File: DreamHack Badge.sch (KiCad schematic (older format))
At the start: 11 parts, among them J2 Conn_01x14_Female, J4 Conn_01x04_Female, U1 ESP32-WROOM-32

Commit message: fixed footprints
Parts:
- J2: footprint (none) -> Pin_Headers:Pin_Header_Straight_1x14_Pitch2.54mm
- J4: footprint (none) -> Pin_Headers:Pin_Header_Straight_1x04_Pitch2.54mm
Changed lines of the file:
@@
 $EndComp
 $Comp
-L power:+3.3V #PWR?
+L power:+3.3V #PWR0101
 U 1 1 5CF7473F
 P 2400 1950
-F 0 "#PWR?" H 2400 1800 50  0001 C CNN
+F 0 "#PWR0101" H 2400 1800 50  0001 C CNN
 F 1 "+3.3V" H 2415 2123 50  0000 C CNN
 F 2 "" H 2400 1950 50  0001 C CNN
@@
 $EndComp
 $Comp
-L power:GND #PWR?
+L power:GND #PWR0102
 U 1 1 5CF74DDF
 P 3650 5550
-F 0 "#PWR?" H 3650 5300 50  0001 C CNN
+F 0 "#PWR0102" H 3650 5300 50  0001 C CNN
 F 1 "GND" H 3655 5377 50  0000 C CNN
 F 2 "" H 3650 5550 50  0001 C CNN
@@
 F 0 "J2" H 6228 2126 50  0000 L CNN
 F 1 "Conn_01x14_Female" H 6228 2035 50  0000 L CNN
-F 2 "" H 6200 2150 50  0001 C CNN
+F 2 "Pin_Headers:Pin_Header_Straight_1x14_Pitch2.54mm" H 6200 2150 50  0001 C CNN
 F 3 "~" H 6200 2150 50  0001 C CNN
 	1    6200 2150
@@
 Connection ~ 8400 4800
 $Comp
-L power:GND #PWR?
+L power:GND #PWR0103
 U 1 1 5CF8F9AB
 P 5750 5850
-F 0 "#PWR?" H 5750 5600 50  0001 C CNN
+F 0 "#PWR0103" H 5750 5600 50  0001 C CNN
 F 1 "GND" H 5755 5677 50  0000 C CNN
 F 2 "" H 5750 5850 50  0001 C CNN
@@
 Connection ~ 9300 4200
 $Comp
-L power:+3.3V #PWR?
+L power:+3.3V #PWR0104
 U 1 1 5CF95312
 P 10050 5250
-F 0 "#PWR?" H 10050 5100 50  0001 C CNN
+F 0 "#PWR0104" H 10050 5100 50  0001 C CNN
 F 1 "+3.3V" H 10065 5423 50  0000 C CNN
 F 2 "" H 10050 5250 50  0001 C CNN
@@
 	3650 5350 3650 5550
 $Comp
-L power:GND #PWR?
+L power:GND #PWR0105
 U 1 1 5CF9CC42
 P 5450 1650
-F 0 "#PWR?" H 5450 1400 50  0001 C CNN
+F 0 "#PWR0105" H 5450 1400 50  0001 C CNN
 F 1 "GND" H 5455 1477 50  0000 C CNN
 F 2 "" H 5450 1650 50  0001 C CNN
@@
 F 0 "J4" H 6228 3376 50  0000 L CNN
 F 1 "Conn_01x04_Female" H 6228 3285 50  0000 L CNN
-F 2 "" H 6200 3400 50  0001 C CNN
+F 2 "Pin_Headers:Pin_Header_Straight_1x04_Pitch2.54mm" H 6200 3400 50  0001 C CNN
 F 3 "~" H 6200 3400 50  0001 C CNN
 	1    6200 3400

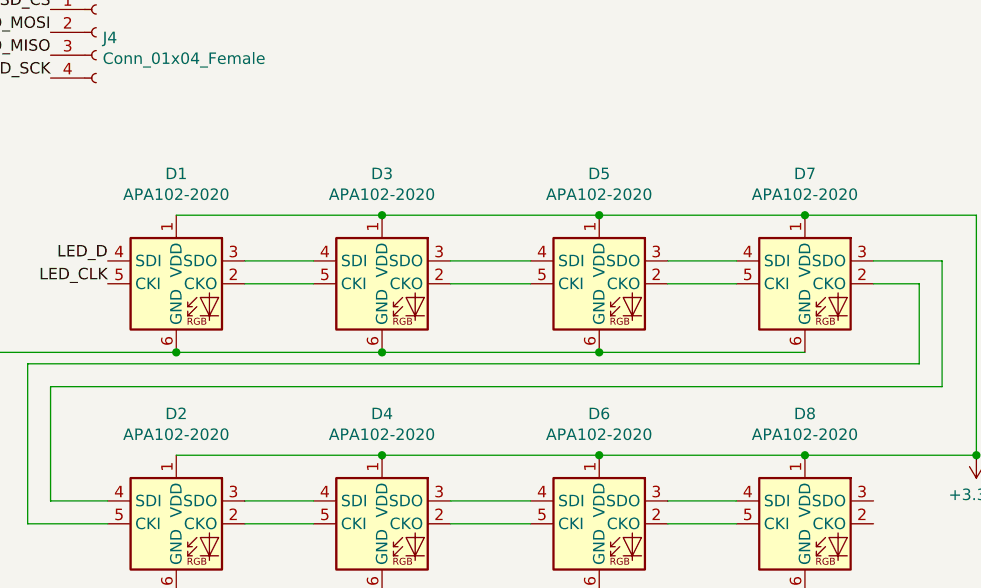
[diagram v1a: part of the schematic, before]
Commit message: fixed apa102 refs
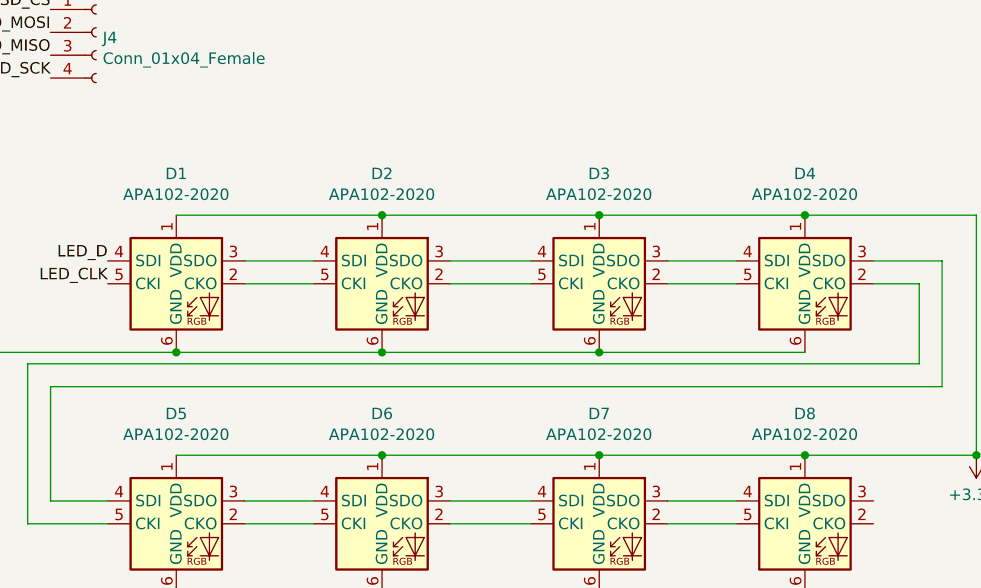
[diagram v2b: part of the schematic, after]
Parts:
- renumbered D3 to D2, D5 to D3, D7 to D4, D2 to D5, D4 to D6, D6 to D7
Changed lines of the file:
@@
 $EndComp
 $Comp
-L LED:APA102-2020 D3
+L LED:APA102-2020 D2
 U 1 1 5CF435C6
 P 7450 4500
-F 0 "D3" H 7450 4981 50  0000 C CNN
+F 0 "D2" H 7450 4981 50  0000 C CNN
 F 1 "APA102-2020" H 7450 4890 50  0000 C CNN
 F 2 "LED_SMD:LED-APA102-2020" H 7500 4200 50  0001 L TNN
@@
 $EndComp
 $Comp
-L LED:APA102-2020 D5
+L LED:APA102-2020 D3
 U 1 1 5CF440DC
 P 8400 4500
-F 0 "D5" H 8400 4981 50  0000 C CNN
+F 0 "D3" H 8400 4981 50  0000 C CNN
 F 1 "APA102-2020" H 8400 4890 50  0000 C CNN
 F 2 "LED_SMD:LED-APA102-2020" H 8450 4200 50  0001 L TNN
@@
 $EndComp
 $Comp
-L LED:APA102-2020 D7
+L LED:APA102-2020 D4
 U 1 1 5CF44F4F
 P 9300 4500
-F 0 "D7" H 9300 4981 50  0000 C CNN
+F 0 "D4" H 9300 4981 50  0000 C CNN
 F 1 "APA102-2020" H 9300 4890 50  0000 C CNN
 F 2 "LED_SMD:LED-APA102-2020" H 9350 4200 50  0001 L TNN
@@
 $EndComp
 $Comp
-L LED:APA102-2020 D2
+L LED:APA102-2020 D5
 U 1 1 5CF4E50D
 P 6550 5550
-F 0 "D2" H 6550 6031 50  0000 C CNN
+F 0 "D5" H 6550 6031 50  0000 C CNN
 F 1 "APA102-2020" H 6550 5940 50  0000 C CNN
 F 2 "LED_SMD:LED-APA102-2020" H 6600 5250 50  0001 L TNN
@@
 $EndComp
 $Comp
-L LED:APA102-2020 D4
+L LED:APA102-2020 D6
 U 1 1 5CF4E513
 P 7450 5550
-F 0 "D4" H 7450 6031 50  0000 C CNN
+F 0 "D6" H 7450 6031 50  0000 C CNN
 F 1 "APA102-2020" H 7450 5940 50  0000 C CNN
 F 2 "LED_SMD:LED-APA102-2020" H 7500 5250 50  0001 L TNN
@@
 $EndComp
 $Comp
-L LED:APA102-2020 D6
+L LED:APA102-2020 D7
 U 1 1 5CF4E519
 P 8400 5550
-F 0 "D6" H 8400 6031 50  0000 C CNN
+F 0 "D7" H 8400 6031 50  0000 C CNN
 F 1 "APA102-2020" H 8400 5940 50  0000 C CNN
 F 2 "LED_SMD:LED-APA102-2020" H 8450 5250 50  0001 L TNN

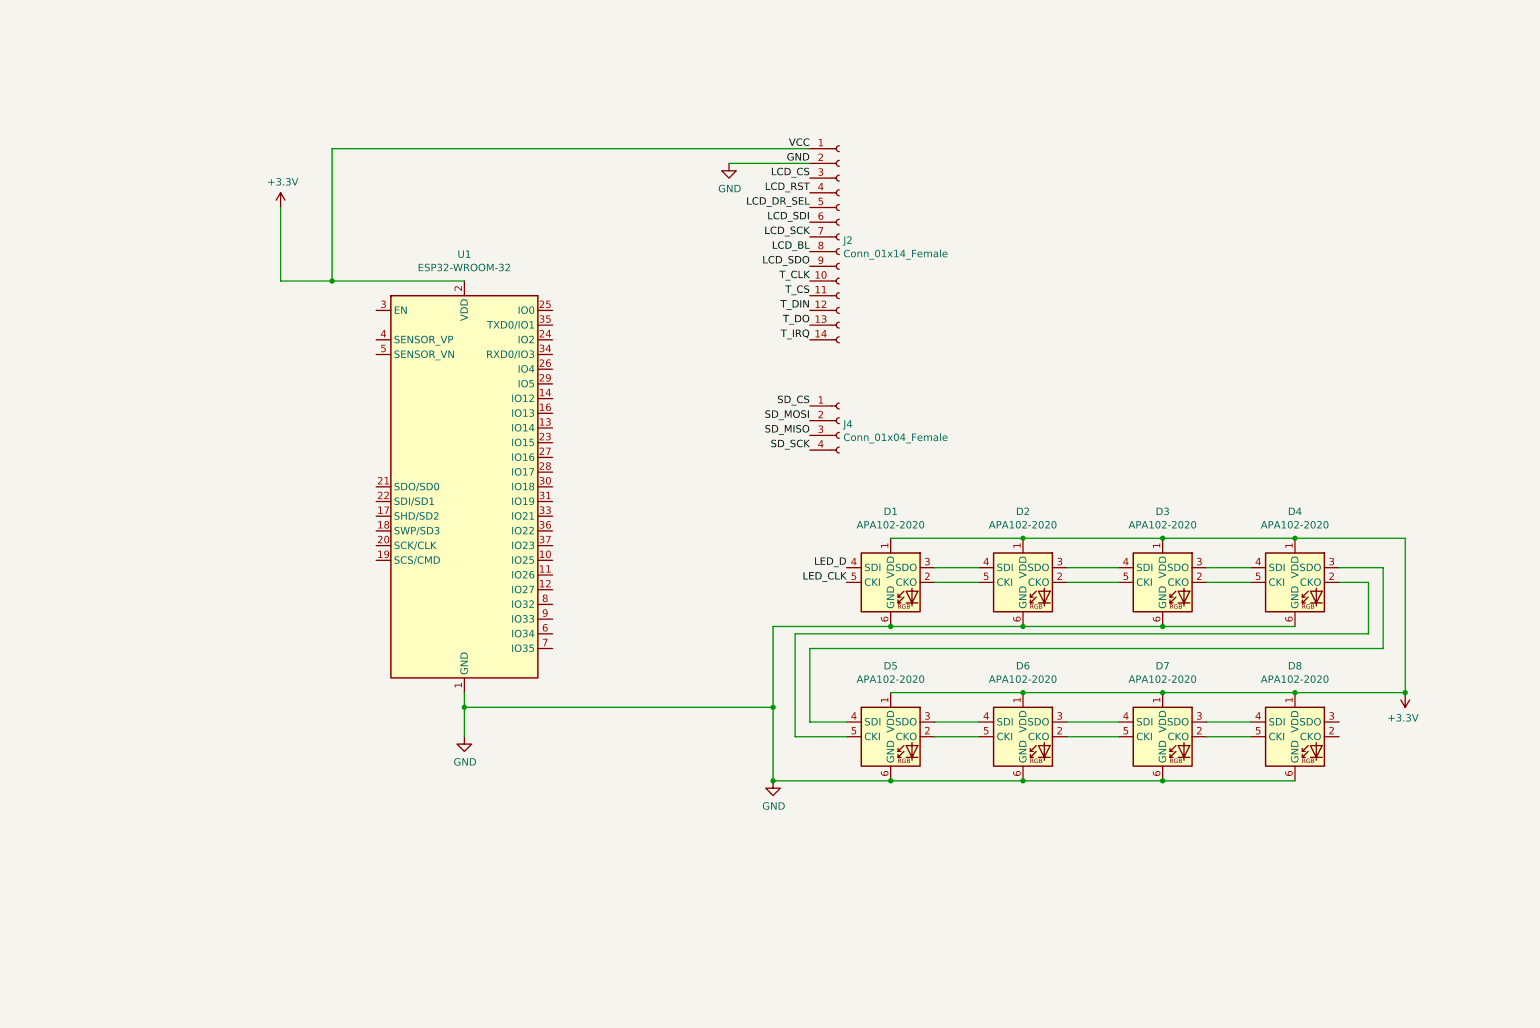
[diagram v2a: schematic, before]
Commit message: updated schematic, added power side
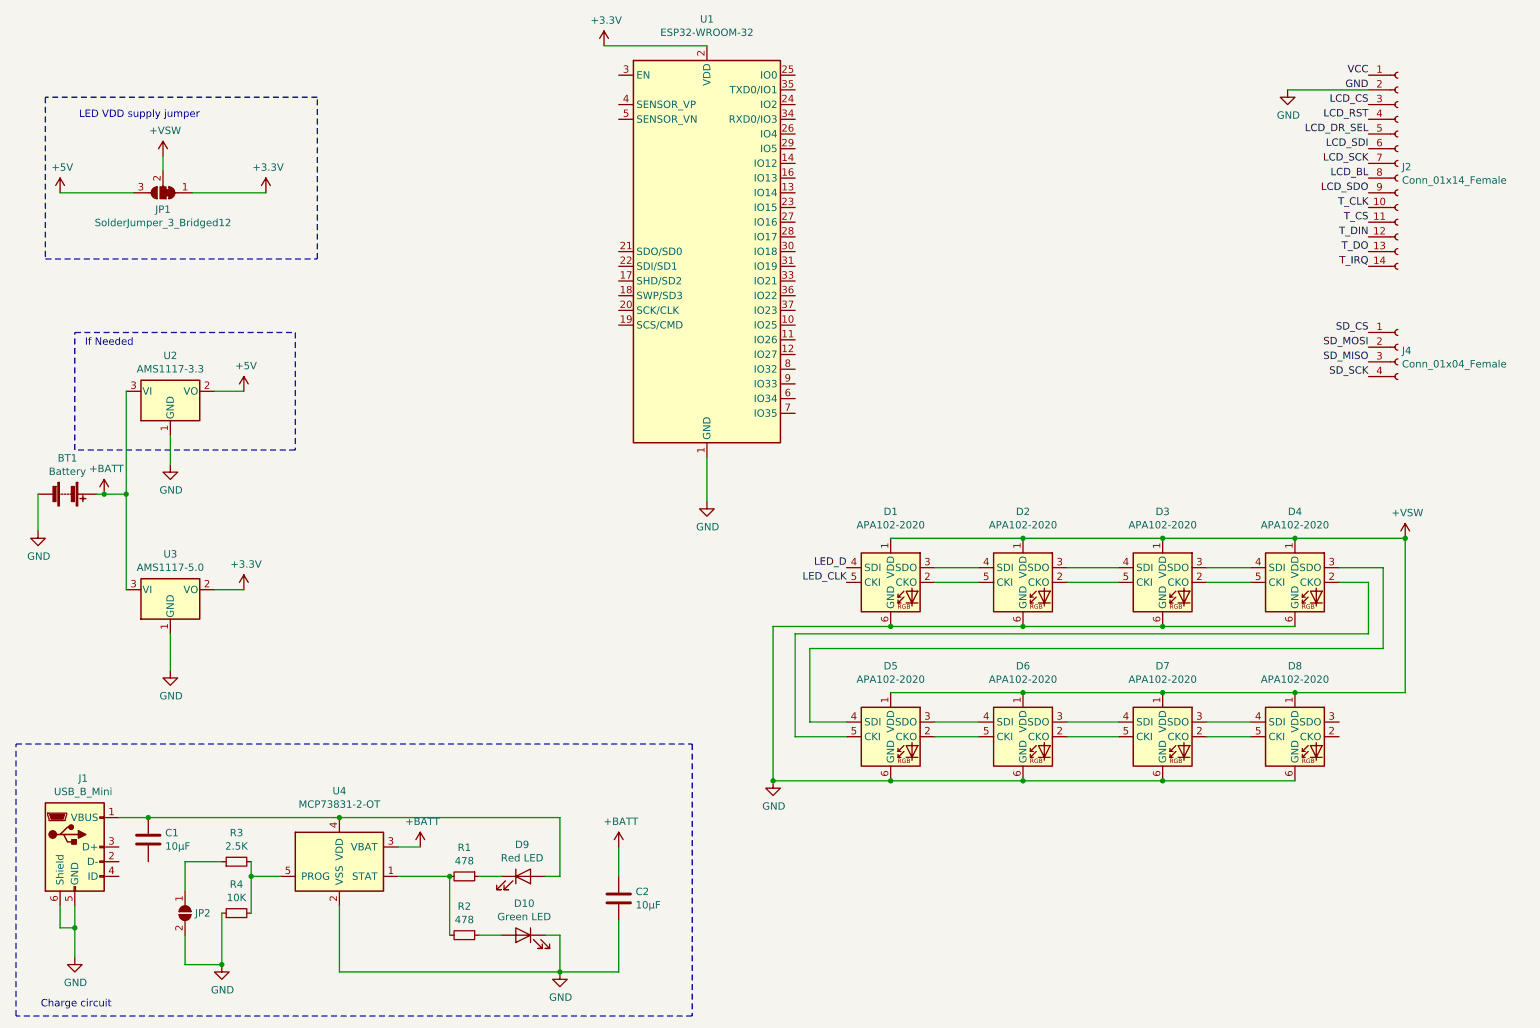
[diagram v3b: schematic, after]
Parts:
- added BT1: Battery, symbol Device:Battery
- added C1, C2: 10μF, symbol Device:C
- added D10: Green LED, symbol Device:LED
- added D9: Red LED, symbol Device:LED
- added J1: USB_B_Mini, symbol Connector:USB_B_Mini
- added JP1: SolderJumper_3_Bridged12, symbol Jumper:SolderJumper_3_Bridged12
- added JP2: SolderJumper_2_Open, symbol Jumper:SolderJumper_2_Open
- added R1, R2: 478, symbol Device:R_Small
- added R3: 2.5K, symbol Device:R_Small
- added R4: 10K, symbol Device:R_Small
- added U2: AMS1117-3.3, Package_TO_SOT_SMD:SOT-223-3_TabPin2, symbol Regulator_Linear:AMS1117-3.3
- added U3: AMS1117-5.0, Package_TO_SOT_SMD:SOT-223-3_TabPin2, symbol Regulator_Linear:AMS1117-5.0
- added U4: MCP73831-2-OT, Package_TO_SOT_SMD:SOT-23-5, symbol Battery_Management:MCP73831-2-OT
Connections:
- net +3V3: now also JP1.1 (A), U3.2 (VO); no longer D1.1 (VDD), D2.1 (VDD), D3.1 (VDD), D4.1 (VDD), D5.1 (VDD), D6.1 (VDD), D7.1 (VDD), D8.1 (VDD), J2.1 (Pin_1)
- net GND: now also BT1.2 (-), C2.2, D10.1 (K), J1.5 (GND), J1.6 (Shield), JP2.2 (B), R4.1, U2.1 (GND), U3.1 (GND), U4.2 (VSS)
- new net: C1.1, D9.2 (A), J1.1 (VBUS), U4.4 (VDD)
- new net: R1.2, R2.2, U4.1 (STAT)
- new net: R3.2, R4.2, U4.5 (PROG)
- new net: D9.1 (K), R1.1
- new net: D10.2 (A), R2.1
- new net: JP2.1 (A), R3.1
- new net +5V: JP1.3 (B), U2.2 (VO)
- new net +BATT: BT1.1 (+), C2.1, U2.3 (VI), U3.3 (VI), U4.3 (VBAT)
- new net +VSW: D1.1 (VDD), D2.1 (VDD), D3.1 (VDD), D4.1 (VDD), D5.1 (VDD), D6.1 (VDD), D7.1 (VDD), D8.1 (VDD), JP1.2 (C)
- new net VCC: J2.1 (Pin_1)
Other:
- note added: "Charge circuit"
- note added: "If Needed"
- note added: "LED VDD supply jumper"
- moved on the sheet: J2, J4, U1

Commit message: fixed footprints
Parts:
- BT1: footprint (none) -> Connector_JST:JST_PH_S2B-PH-K_1x02_P2.00mm_Horizontal
- C1, C2: footprint (none) -> Capacitors_SMD:C_0805_HandSoldering
- D10, D9: footprint (none) -> LEDs:LED_0805_HandSoldering
- J1: footprint (none) -> Connectors:USB_Mini-B
- JP1: footprint (none) -> Jumper:SolderJumper-3_P1.3mm_Bridged12_RoundedPad1.0x1.5mm
- JP2: footprint (none) -> Jumper:SolderJumper-2_P1.3mm_Open_RoundedPad1.0x1.5mm
- R1, R2, R3, R4: footprint (none) -> Resistors_SMD:R_0805_HandSoldering
- U2, U3: footprint Package_TO_SOT_SMD:SOT-223-3_TabPin2 -> TO_SOT_Packages_SMD:SOT-223-3_TabPin2
- U4: footprint Package_TO_SOT_SMD:SOT-23-5 -> TO_SOT_Packages_SMD:TSOT-23-5_HandSoldering
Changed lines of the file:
@@
 F 0 "BT1" V 705 3900 50  0000 C CNN
 F 1 "Battery" V 796 3900 50  0000 C CNN
-F 2 "" V 950 3960 50  0001 C CNN
+F 2 "Connector_JST:JST_PH_S2B-PH-K_1x02_P2.00mm_Horizontal" V 950 3960 50  0001 C CNN
 F 3 "~" V 950 3960 50  0001 C CNN
 	1    950  3900
@@
 F 0 "J1" H 1057 6767 50  0000 C CNN
 F 1 "USB_B_Mini" H 1057 6676 50  0000 C CNN
-F 2 "" H 1150 6250 50  0001 C CNN
+F 2 "Connectors:USB_Mini-B" H 1150 6250 50  0001 C CNN
 F 3 "~" H 1150 6250 50  0001 C CNN
 	1    1000 6300
@@
 F 0 "U4" H 2800 6881 50  0000 C CNN
 F 1 "MCP73831-2-OT" H 2800 6790 50  0000 C CNN
-F 2 "Package_TO_SOT_SMD:SOT-23-5" H 2850 6150 50  0001 L CIN
+F 2 "TO_SOT_Packages_SMD:TSOT-23-5_HandSoldering" H 2850 6150 50  0001 L CIN
 F 3 "http://ww1.microchip.com/downloads/en/DeviceDoc/20001984g.pdf" H 2650 6350 50  0001 C CNN
 	1    2800 6400
@@
 F 0 "D9" H 4043 6716 50  0000 C CNN
 F 1 "Red LED" H 4043 6625 50  0000 C CNN
-F 2 "" H 4050 6500 50  0001 C CNN
+F 2 "LEDs:LED_0805_HandSoldering" H 4050 6500 50  0001 C CNN
 F 3 "~" H 4050 6500 50  0001 C CNN
 	1    4050 6500
@@
 F 0 "D10" H 4043 7116 50  0000 C CNN
 F 1 "Green LED" H 4043 7025 50  0000 C CNN
-F 2 "" H 4050 6900 50  0001 C CNN
+F 2 "LEDs:LED_0805_HandSoldering" H 4050 6900 50  0001 C CNN
 F 3 "~" H 4050 6900 50  0001 C CNN
 	1    4050 6900
@@
 F 0 "JP1" H 1600 1963 50  0000 C CNN
 F 1 "SolderJumper_3_Bridged12" H 1600 2054 50  0000 C CNN
-F 2 "" H 1600 1850 50  0001 C CNN
+F 2 "Jumper:SolderJumper-3_P1.3mm_Bridged12_RoundedPad1.0x1.5mm" H 1600 1850 50  0001 C CNN
 F 3 "~" H 1600 1850 50  0001 C CNN
 	1    1600 1850
@@
 F 0 "R1" V 3454 6500 50  0000 C CNN
 F 1 "478" V 3545 6500 50  0000 C CNN
-F 2 "" H 3650 6500 50  0001 C CNN
+F 2 "Resistors_SMD:R_0805_HandSoldering" H 3650 6500 50  0001 C CNN
 F 3 "~" H 3650 6500 50  0001 C CNN
 	1    3650 6500
@@
 F 0 "R2" V 3454 6900 50  0000 C CNN
 F 1 "478" V 3545 6900 50  0000 C CNN
-F 2 "" H 3650 6900 50  0001 C CNN
+F 2 "Resistors_SMD:R_0805_HandSoldering" H 3650 6900 50  0001 C CNN
 F 3 "~" H 3650 6900 50  0001 C CNN
 	1    3650 6900
@@
 F 0 "R3" V 2296 6400 50  0000 C CNN
 F 1 "2.5K" V 2205 6400 50  0000 C CNN
-F 2 "" H 2100 6400 50  0001 C CNN
+F 2 "Resistors_SMD:R_0805_HandSoldering" H 2100 6400 50  0001 C CNN
 F 3 "~" H 2100 6400 50  0001 C CNN
 	1    2100 6400
@@
 F 0 "R4" V 2296 6750 50  0000 C CNN
 F 1 "10K" V 2205 6750 50  0000 C CNN
-F 2 "" H 2100 6750 50  0001 C CNN
+F 2 "Resistors_SMD:R_0805_HandSoldering" H 2100 6750 50  0001 C CNN
 F 3 "~" H 2100 6750 50  0001 C CNN
 	1    2100 6750
@@
 F 0 "JP2" V 1750 6818 50  0000 L CNN
 F 1 "SolderJumper_2_Open" V 1795 6818 50  0001 L CNN
-F 2 "" H 1750 6750 50  0001 C CNN
+F 2 "Jumper:SolderJumper-2_P1.3mm_Open_RoundedPad1.0x1.5mm" H 1750 6750 50  0001 C CNN
 F 3 "~" H 1750 6750 50  0001 C CNN
 	1    1750 6750
@@
 F 0 "C1" H 1615 6296 50  0000 L CNN
 F 1 "10μF" H 1615 6205 50  0000 L CNN
-F 2 "" H 1538 6100 50  0001 C CNN
+F 2 "Capacitors_SMD:C_0805_HandSoldering" H 1538 6100 50  0001 C CNN
 F 3 "~" H 1500 6250 50  0001 C CNN
 	1    1500 6250
@@
 F 0 "C2" H 4815 6696 50  0000 L CNN
 F 1 "10μF" H 4815 6605 50  0000 L CNN
-F 2 "" H 4738 6500 50  0001 C CNN
+F 2 "Capacitors_SMD:C_0805_HandSoldering" H 4738 6500 50  0001 C CNN
 F 3 "~" H 4700 6650 50  0001 C CNN
 	1    4700 6650
@@
 F 0 "U3" H 1650 4792 50  0000 C CNN
 F 1 "AMS1117-5.0" H 1650 4701 50  0000 C CNN
-F 2 "Package_TO_SOT_SMD:SOT-223-3_TabPin2" H 1650 4750 50  0001 C CNN
+F 2 "TO_SOT_Packages_SMD:SOT-223-3_TabPin2" H 1650 4750 50  0001 C CNN
 F 3 "http://www.advanced-monolithic.com/pdf/ds1117.pdf" H 1750 4300 50  0001 C CNN
 	1    1650 4550
@@
 F 0 "U2" H 1650 3442 50  0000 C CNN
 F 1 "AMS1117-3.3" H 1650 3351 50  0000 C CNN
-F 2 "Package_TO_SOT_SMD:SOT-223-3_TabPin2" H 1650 3400 50  0001 C CNN
+F 2 "TO_SOT_Packages_SMD:SOT-223-3_TabPin2" H 1650 3400 50  0001 C CNN
 F 3 "http://www.advanced-monolithic.com/pdf/ds1117.pdf" H 1750 2950 50  0001 C CNN
 	1    1650 3200
